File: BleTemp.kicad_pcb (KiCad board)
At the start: 2 copper layers, 50 x 30 mm, 28 parts, among them U1 NRF52832-QFAA-R, X1 32MHz, X2 32.768KHz

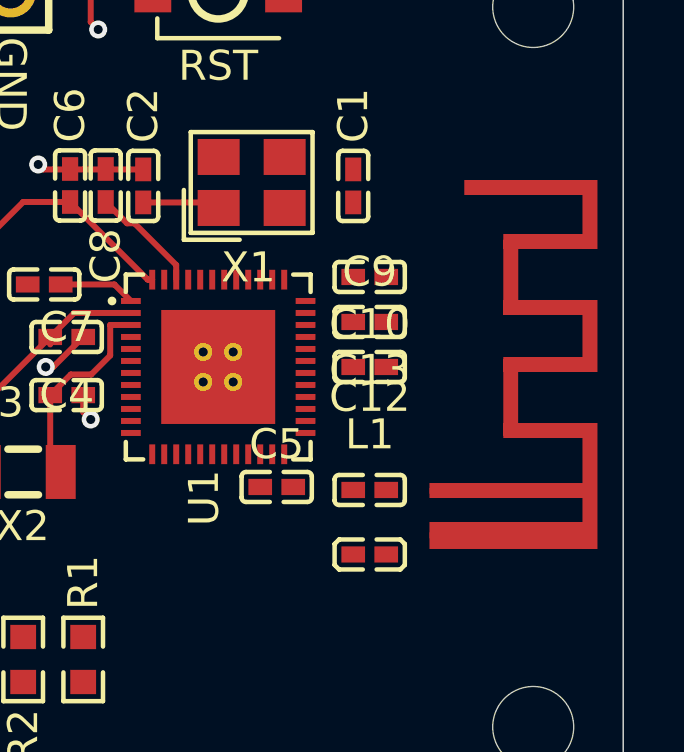
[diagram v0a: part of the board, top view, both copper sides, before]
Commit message: connect antenna
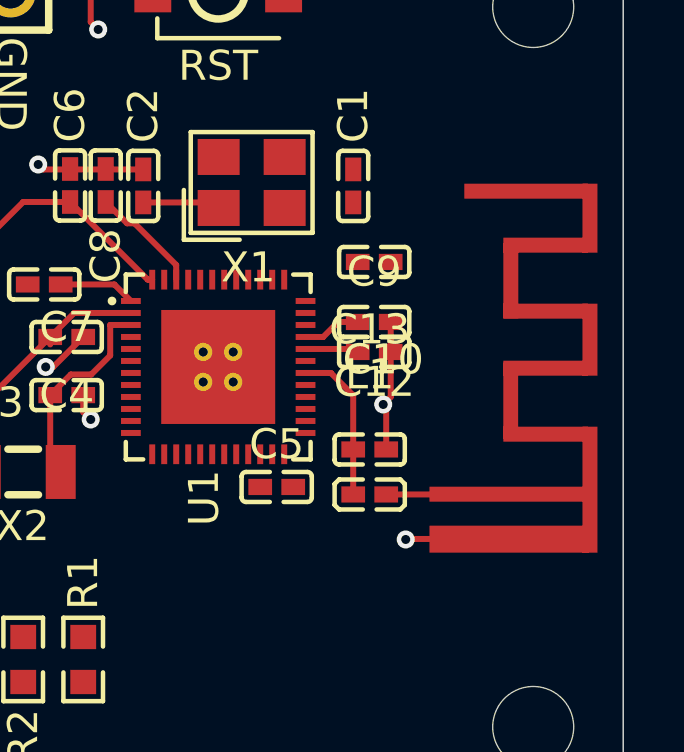
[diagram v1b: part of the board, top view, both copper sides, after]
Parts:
- moved L1 2.00 mm to (135.1, 48.8)
- moved C13 1.35 mm to (135.1, 47.2)
- moved C10 0.52 mm to (135.2, 44.0)
- moved C12 0.52 mm to (135.2, 41.0)
- moved C9 0.15 mm to (135.2, 43.0)
- moved ANT 0.12 mm to (140.0, 44.6)
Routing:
- net GND: track 17.0 -> 22.3 mm, vias 6 -> 8
- net Net-(U1-ANT): track 0.00 -> 5.20 mm
- net Net-(U1-DEC3): track 0.00 -> 1.95 mm
- net Net-(U1-DEC2): track 0.00 -> 1.78 mm
- net Net-(AE1-PCB_Trace): track 0.00 -> 1.54 mm
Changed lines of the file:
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@@
 	(footprint "wch-antenna:ANT-F-1-2.4G-1.6MM-FR4-WCH"
 		(layer "F.Cu")
-		(at 140 44.5 -90)
+		(at 140 44.6225 -90)
 		(descr "2.4GHz PCB antenna for 1.6mm FR4 boards. Design provided by WCH. Website: wch-ic.com")
 		(tags "Antenna, WCH")
@@
 	(footprint "easyeda2kicad:C0402"
 		(layer "F.Cu")
-		(at 135.05 41.5 180)
+		(at 135.2 41 180)
 		(property "Reference" "C12"
 			(at 0 -4 0)
@@
 	(footprint "easyeda2kicad:C0402"
 		(layer "F.Cu")
-		(at 135.05 43 180)
+		(at 135.2 43 180)
 		(property "Reference" "C9"
 			(at 0 1.67325 0)
@@
 	(footprint "easyeda2kicad:C0402"
 		(layer "F.Cu")
-		(at 135.05 48.6)
+		(at 135.05 47.25)
 		(property "Reference" "C13"
 			(at 0 -4 0)
@@
 	(footprint "easyeda2kicad:L0402"
 		(layer "F.Cu")
-		(at 135.05 50.75)
+		(at 135.05 48.75)
 		(property "Reference" "L1"
 			(at 0 -4 0)
@@
 	(footprint "easyeda2kicad:C0402"
 		(layer "F.Cu")
-		(at 135.05 44.5 180)
+		(at 135.2 44 180)
 		(property "Reference" "C10"
-			(at 0 1.42325 0)
+			(at -0.3 -0.25 0)
 			(layer "F.SilkS")
 			(effects
@@
 	)
 	(segment
+		(start 135.75 43)
+		(end 135.75 45.5)
+		(width 0.2)
+		(layer "F.Cu")
+		(net 1)
+	)
+	(segment
 		(start 125.75 33)
 		(end 126 33.25)
@@
 	)
 	(segment
+		(start 136.2672 50.2328)
+		(end 136.25 50.25)
+		(width 0.2)
+		(layer "F.Cu")
+		(net 1)
+	)
+	(segment
+		(start 135.6 45.85)
+		(end 135.5 45.75)
+		(width 0.2)
+		(layer "F.Cu")
+		(net 1)
+	)
+	(segment
 		(start 99.25 43.25)
 		(end 99.5 43.25)
@@
 	)
 	(segment
+		(start 135.75 45.5)
+		(end 135.5 45.75)
+		(width 0.2)
+		(layer "F.Cu")
+		(net 1)
+	)
+	(segment
 		(start 125.75 32)
 		(end 127.82 32)
@@
 	)
 	(segment
+		(start 135.6 47.25)
+		(end 135.6 45.85)
+		(width 0.2)
+		(layer "F.Cu")
+		(net 1)
+	)
+	(segment
+		(start 137.1425 50.2328)
+		(end 136.2672 50.2328)
+		(width 0.2)
+		(layer "F.Cu")
+		(net 1)
+	)
+	(segment
 		(start 123.08 32)
 		(end 125.75 32)
@@
 	)
 	(via
+		(at 136.25 50.25)
+		(size 0.6)
+		(drill 0.3)
+		(layers "F.Cu" "B.Cu")
+		(net 1)
+	)
+	(via
 		(at 119.5 51.5)
 		(size 0.6)
@@
 	)
 	(via
+		(at 135.5 45.75)
+		(size 0.6)
+		(drill 0.3)
+		(layers "F.Cu" "B.Cu")
+		(net 1)
+	)
+	(via
 		(at 99.5 43.25)
 		(size 0.6)
@@
 	)
 	(segment
+		(start 137.1425 48.75)
+		(end 135.6 48.75)
+		(width 0.2)
+		(layer "F.Cu")
+		(net 2)
+	)
+	(segment
 		(start 123.5 39)
 		(end 125.062501 39)
@@
 		(net 9)
 	)
+	(segment
+		(start 132.91 43.5)
+		(end 133.5 43.5)
+		(width 0.2)
+		(layer "F.Cu")
+		(net 10)
+	)
+	(segment
+		(start 133.5 43.5)
+		(end 134 43)
+		(width 0.2)
+		(layer "F.Cu")
+		(net 10)
+	)
+	(segment
+		(start 134 43)
+		(end 134.65 43)
+		(width 0.2)
+		(layer "F.Cu")
+		(net 10)
+	)
+	(segment
+		(start 132.91 43.9)
+		(end 134.55 43.9)
+		(width 0.2)
+		(layer "F.Cu")
+		(net 11)
+	)
+	(segment
+		(start 134.55 43.9)
+		(end 134.65 44)
+		(width 0.2)
+		(layer "F.Cu")
+		(net 11)
+	)
+	(segment
+		(start 133.755 44.7)
+		(end 132.91 44.7)
+		(width 0.2)
+		(layer "F.Cu")
+		(net 44)
+	)
+	(segment
+		(start 134.5 48.75)
+		(end 134.5 47.25)
+		(width 0.2)
+		(layer "F.Cu")
+		(net 44)
+	)
+	(segment
+		(start 134.5 45.445)
+		(end 133.755 44.7)
+		(width 0.2)
+		(layer "F.Cu")
+		(net 44)
+	)
+	(segment
+		(start 134.5 47.25)
+		(end 134.5 45.445)
+		(width 0.2)
+		(layer "F.Cu")
+		(net 44)
+	)
 	(zone

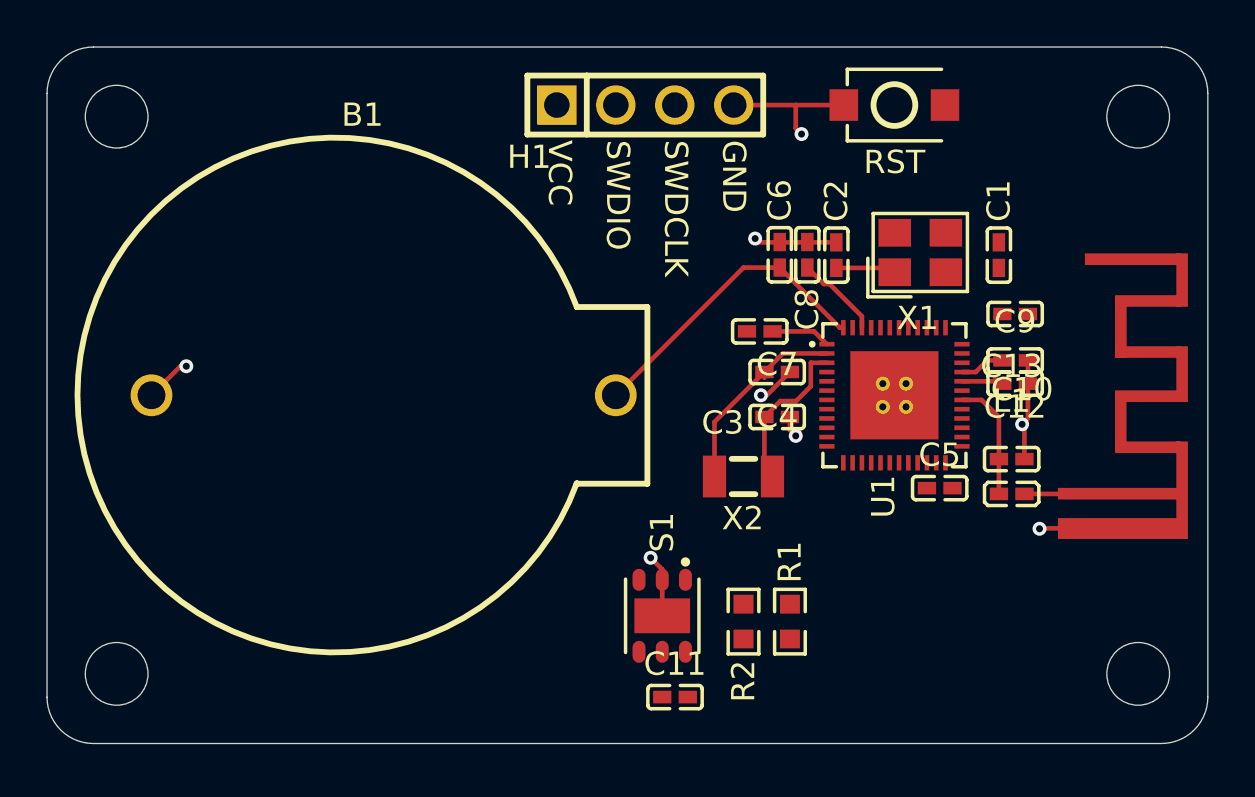
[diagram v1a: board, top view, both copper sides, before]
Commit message: add copper zones
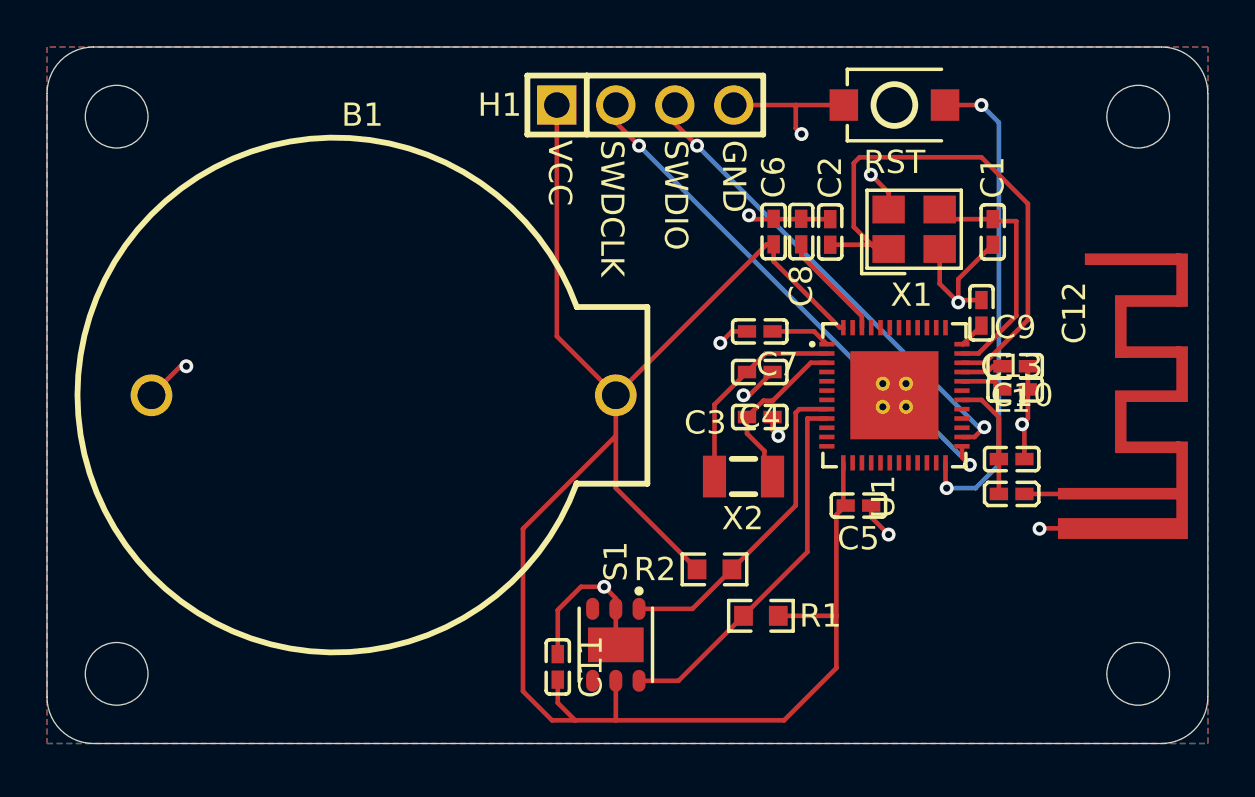
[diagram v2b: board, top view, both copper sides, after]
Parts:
- moved C11 5.21 mm to (115.5, 56.2), turned to -90 degrees
- moved C5 3.58 mm to (128.4, 49.2), turned to 180 degrees
- moved R2 2.57 mm to (122.2, 52.0), turned to 180 degrees
- moved S1 2.36 mm to (118.0, 55.2)
- moved C12 1.45 mm to (133.8, 41.0), turned to -90 degrees
- moved R1 1.27 mm to (124.2, 54.0), turned to 0 degrees
- moved X1 1.03 mm to (130.8, 37.4)
- moved C2 1.03 mm to (127.2, 37.5)
- moved C6 1.03 mm to (124.8, 37.5)
- moved C8 1.03 mm to (126.0, 37.5)
- moved C1 1.03 mm to (134.2, 37.5)
- moved C3 0.75 mm to (124.2, 45.4)
- moved C4 0.75 mm to (124.2, 43.5)
- moved C10 0.25 mm to (135.2, 44.2)
- moved C9 0.25 mm to (135.2, 43.2)
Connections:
- H1 pad 2: SWDIO -> SWDCLK
- H1 pad 3: SWDCLK -> SWDIO
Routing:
- net VCC_3V3: track 13.2 -> 81.0 mm
- net SWDCLK: track 0.00 -> 24.2 mm, vias 0 -> 2
- net Net-(U1-XC1): track 2.59 -> 24.3 mm
- net Net-(U1-P0.21/RESET): track 0.00 -> 20.9 mm, vias 0 -> 2
- net SWDIO: track 0.00 -> 20.6 mm, vias 0 -> 2
- net SCL: track 0.00 -> 16.1 mm
- net GND: track 22.3 -> 37.8 mm, vias 8 -> 12
- net SDA: track 0.00 -> 14.0 mm
- net Net-(U1-XC2): track 0.00 -> 10.6 mm
- net Net-(U1-DEC4): track 3.71 -> 4.67 mm
- added copper zone on B.Cu, net GND
- added copper zone on F.Cu, net GND

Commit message: add traces
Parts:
- moved C12 0.50 mm to (133.2, 41.0)
- moved C13 0.50 mm to (134.6, 47.2)
- moved C3 0.50 mm to (123.7, 45.4)
- moved C4 0.50 mm to (123.7, 43.5)
- moved C7 0.50 mm to (123.7, 41.8)
- moved L1 0.50 mm to (134.6, 48.8)
- moved U1 0.50 mm to (129.5, 44.5)
- moved X2 0.50 mm to (123.0, 48.0)
- moved C5 0.50 mm to (128.0, 49.2)
- moved C10 0.25 mm to (135.2, 44.5)
- moved C9 0.25 mm to (135.2, 43.5)
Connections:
- U1 pad : (no net) -> GND
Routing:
- net GND: track 37.8 -> 43.6 mm, vias 12 -> 24
- net SWDCLK: track 24.2 -> 23.7 mm
- net Net-(U1-P0.21/RESET): track 20.9 -> 21.4 mm
- net Net-(AE1-PCB_Trace): track 1.54 -> 2.04 mm

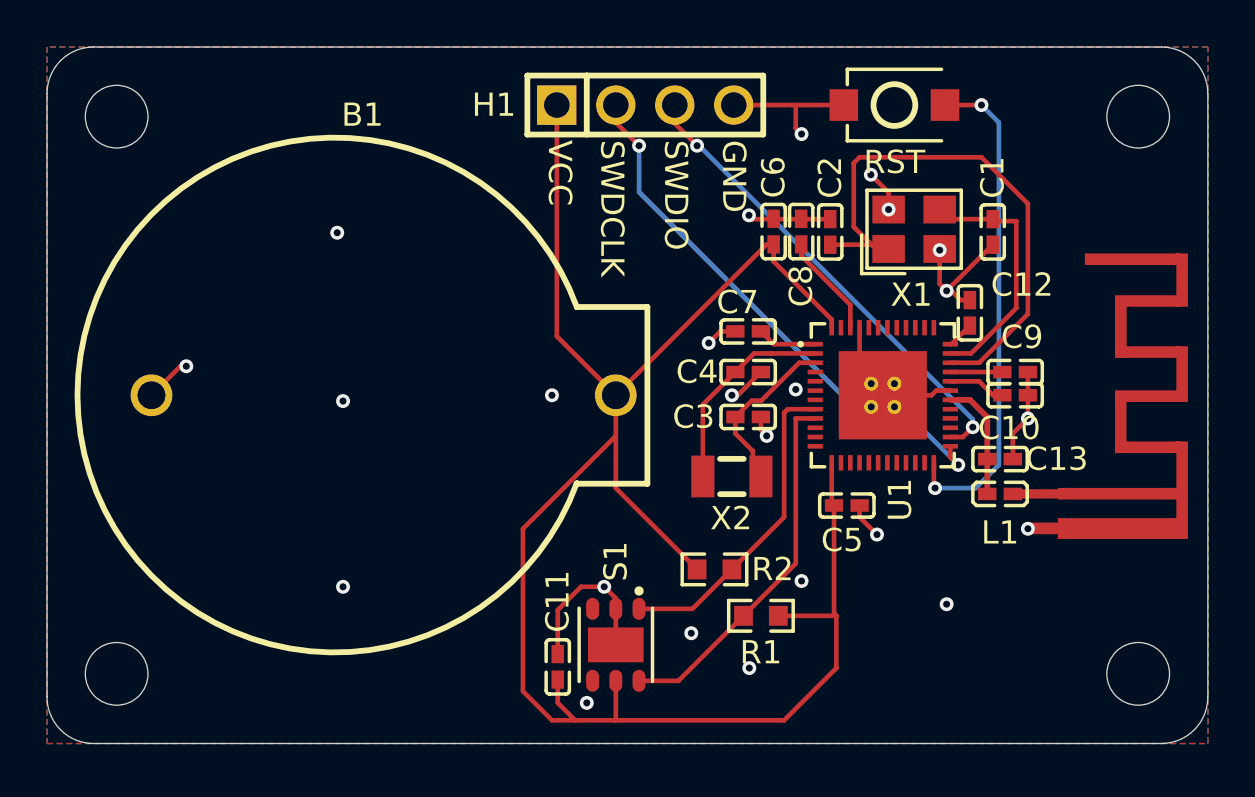
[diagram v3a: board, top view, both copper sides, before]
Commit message: improve antenna connection
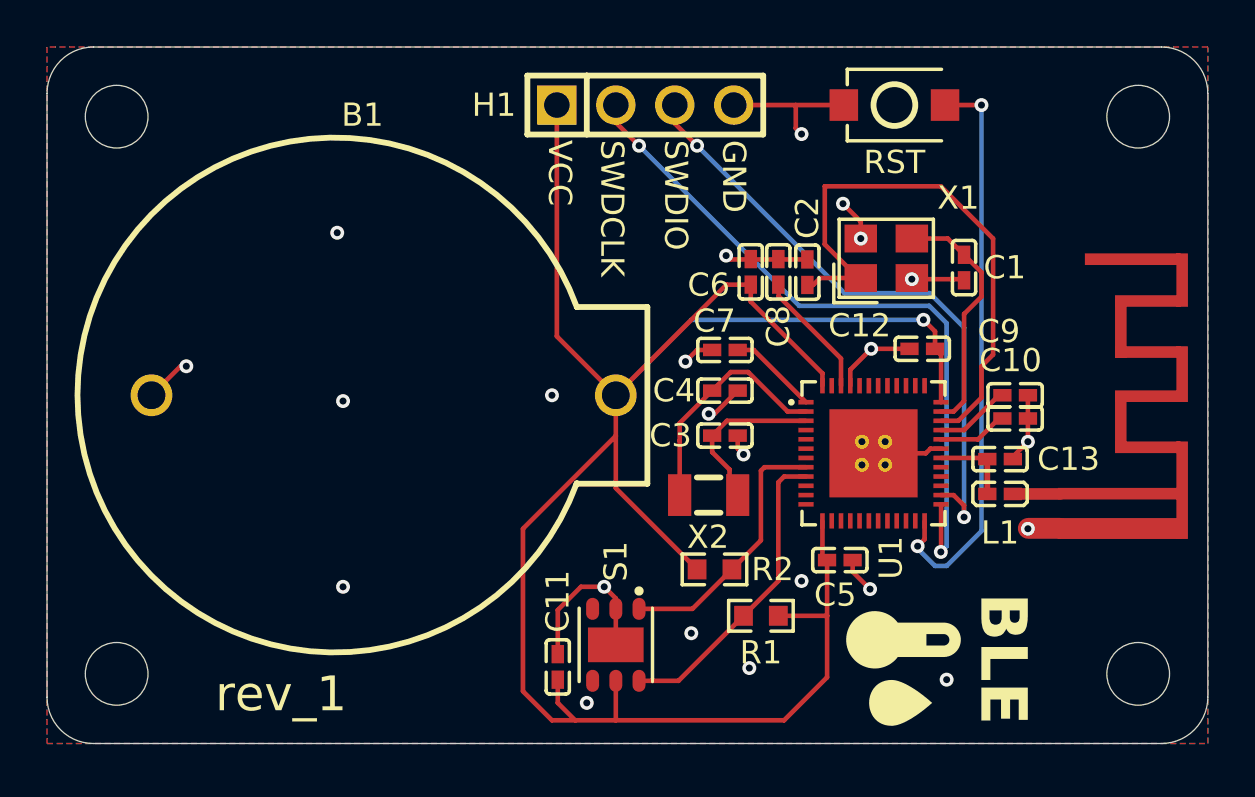
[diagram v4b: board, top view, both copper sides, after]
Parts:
- moved C12 2.57 mm to (131.2, 42.5), turned to 0 degrees
- moved U1 2.53 mm to (129.1, 47.0)
- moved C5 2.37 mm to (127.7, 51.6)
- moved C2 2.00 mm to (126.2, 39.2)
- moved C6 2.00 mm to (123.8, 39.2)
- moved C8 2.00 mm to (125.0, 39.2)
- moved C1 1.97 mm to (133.0, 39.0)
- moved X1 1.73 mm to (129.7, 38.6)
- moved C3 1.28 mm to (122.7, 46.2)
- moved C4 1.28 mm to (122.7, 44.3)
- moved C7 1.28 mm to (122.7, 42.5)
- moved X2 1.28 mm to (122.0, 48.8)
- moved C10 1.00 mm to (135.2, 45.5)
- moved C9 1.00 mm to (135.2, 44.5)
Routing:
- net VCC_3V3: track 80.6 -> 94.5 mm, vias 0 -> 1
- net SWDCLK: track 23.7 -> 30.6 mm
- net SWDIO: track 20.4 -> 26.8 mm
- net GND: track 43.6 -> 39.4 mm, vias 24 -> 23
- net Net-(U1-P0.21/RESET): track 21.4 -> 24.7 mm
- net SCL: track 15.9 -> 13.3 mm
- net SDA: track 13.8 -> 11.5 mm
- net Net-(U1-ANT): track 5.20 -> 3.51 mm
- net Net-(U1-DEC1): track 2.57 -> 3.87 mm
- net Net-(U1-P0.00/XL1): track 8.85 -> 10.2 mm
- net Net-(U1-DEC3): track 2.24 -> 3.26 mm
- net Net-(U1-DEC4): track 4.47 -> 5.47 mm
- net Net-(U1-DEC2): track 2.49 -> 3.01 mm
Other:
- board text added: "BLE"
- board text added: "github.com/MrMarble/ble-sensor"
- board text added: "rev_1"
